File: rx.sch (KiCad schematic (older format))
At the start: 82 parts, among them J5 Conn_Coaxial, Q1 BSS123, Q2 BSS123, Q3 BSS123, Q4 BSS123, Q5 BSS123, Q6 BSS123, T1 Transformer_1P_SS, U12 MMG3H21NT1, U3 SN74CBT3253, U9 LT6231CSB

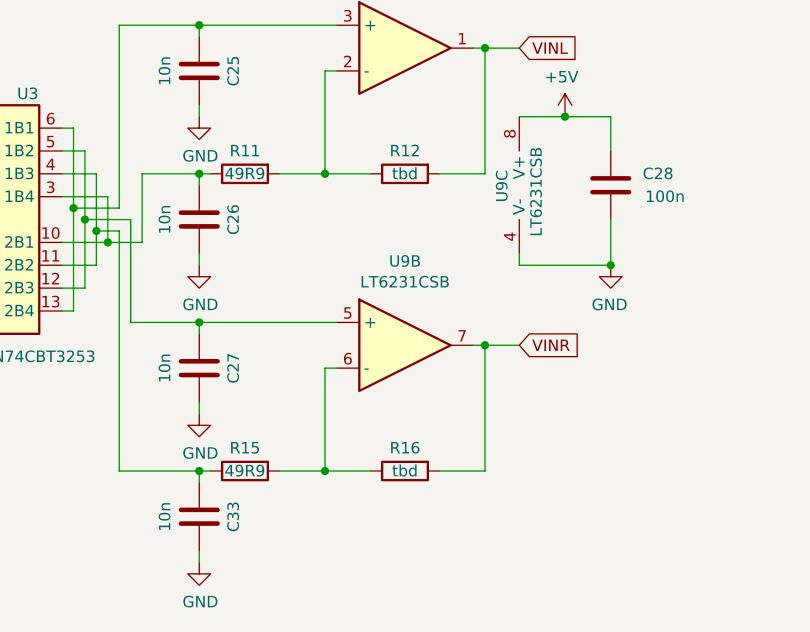
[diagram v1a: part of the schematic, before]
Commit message: Added capacitors to codec's VCOM
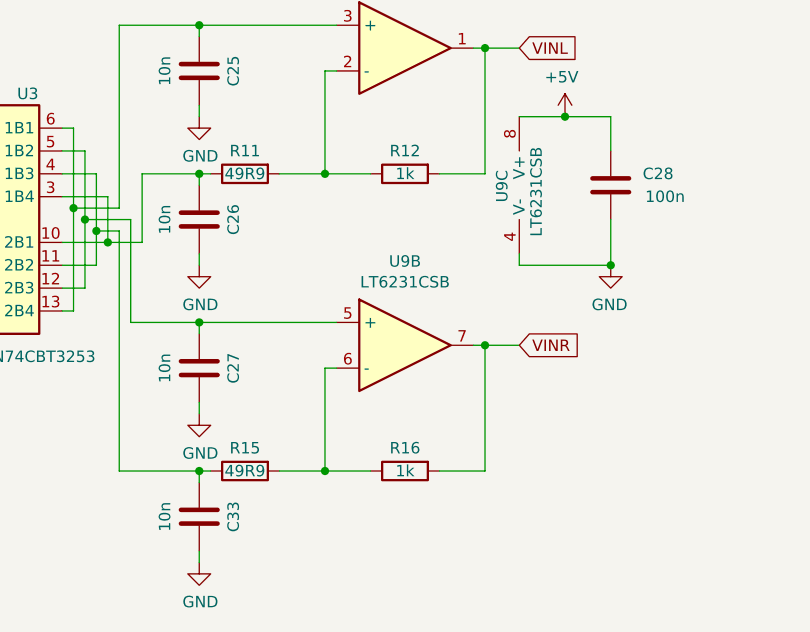
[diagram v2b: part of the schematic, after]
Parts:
- R12, R16: value tbd -> 1k
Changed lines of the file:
@@
 AR Path="/5E9BB9DC/5EB59067" Ref="R12"  Part="1"
 F 0 "R12" V 5450 5700 50  0000 C CNN
-F 1 "tbd" V 5550 5700 50  0000 C CNN
+F 1 "1k" V 5550 5700 50  0000 C CNN
 F 2 "Resistor_SMD:R_0603_1608Metric" V 5480 5700 50  0001 C CNN
 F 3 "~" H 5550 5700 50  0001 C CNN
@@
 AR Path="/5E9BB9DC/5EB71CBB" Ref="R16"  Part="1"
 F 0 "R16" V 5450 7000 50  0000 C CNN
-F 1 "tbd" V 5550 7000 50  0000 C CNN
+F 1 "1k" V 5550 7000 50  0000 C CNN
 F 2 "Resistor_SMD:R_0603_1608Metric" V 5480 7000 50  0001 C CNN
 F 3 "~" H 5550 7000 50  0001 C CNN
